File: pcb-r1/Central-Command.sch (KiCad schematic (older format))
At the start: 16 parts, among them P1 CONN_01X06, P2 CONN_01X02, P3 CONN_01X03, SW1 SW_PUSH, U1 STM32F030C8, Y1 Crystal

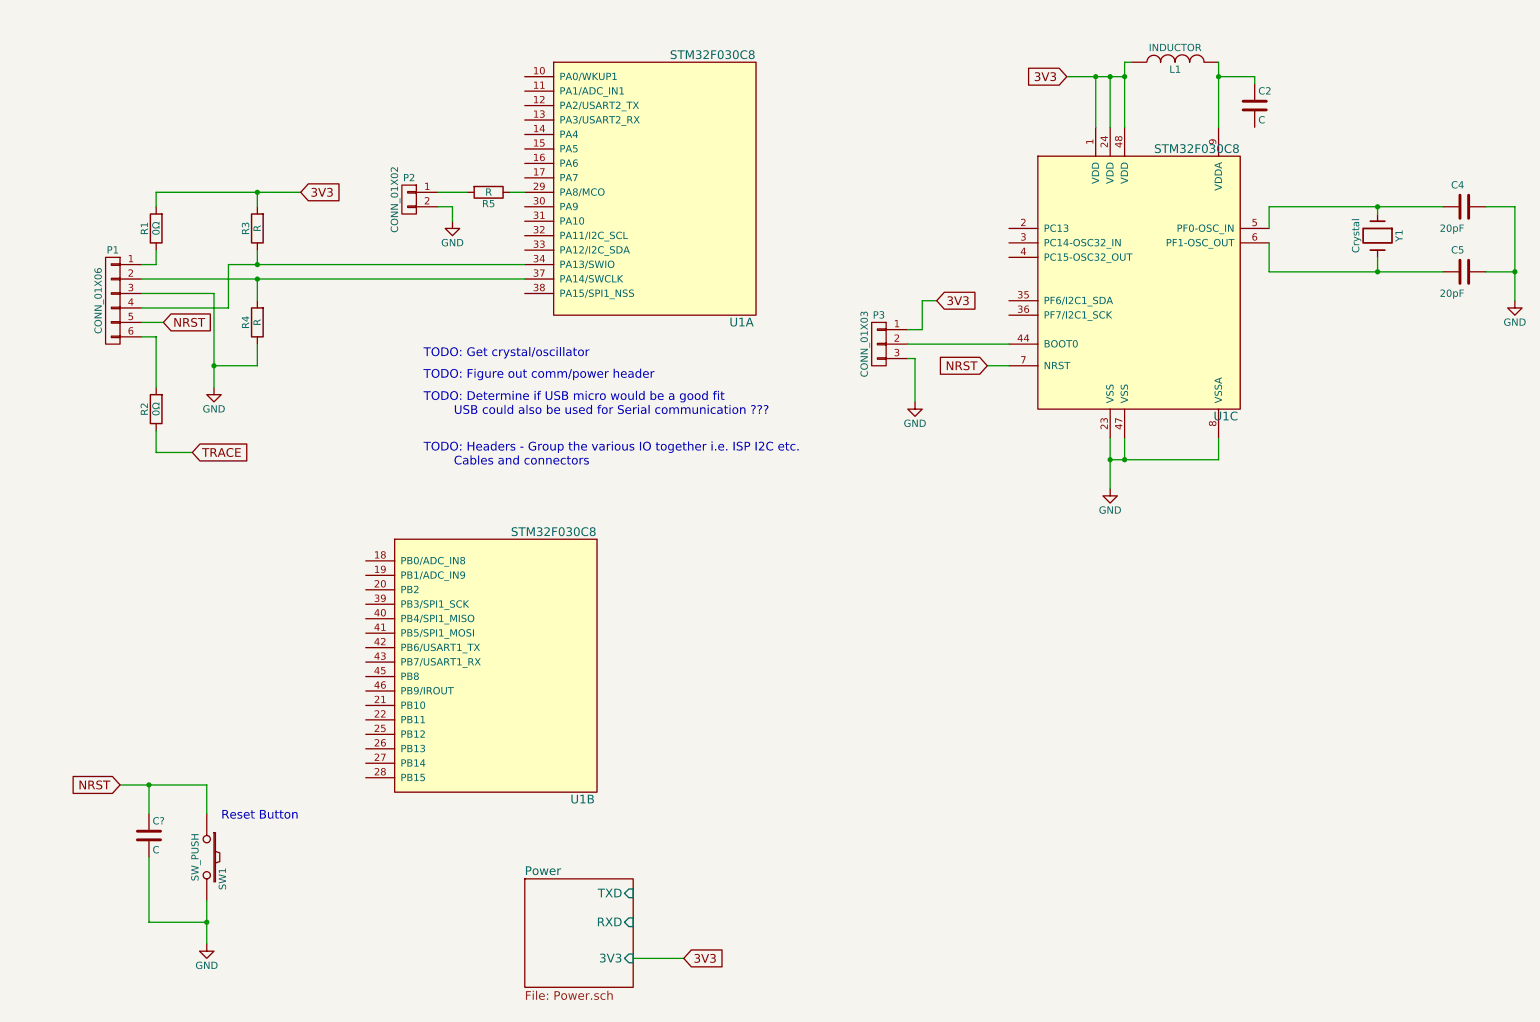
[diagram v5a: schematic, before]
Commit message: Updated the schematic with the latest from CC17
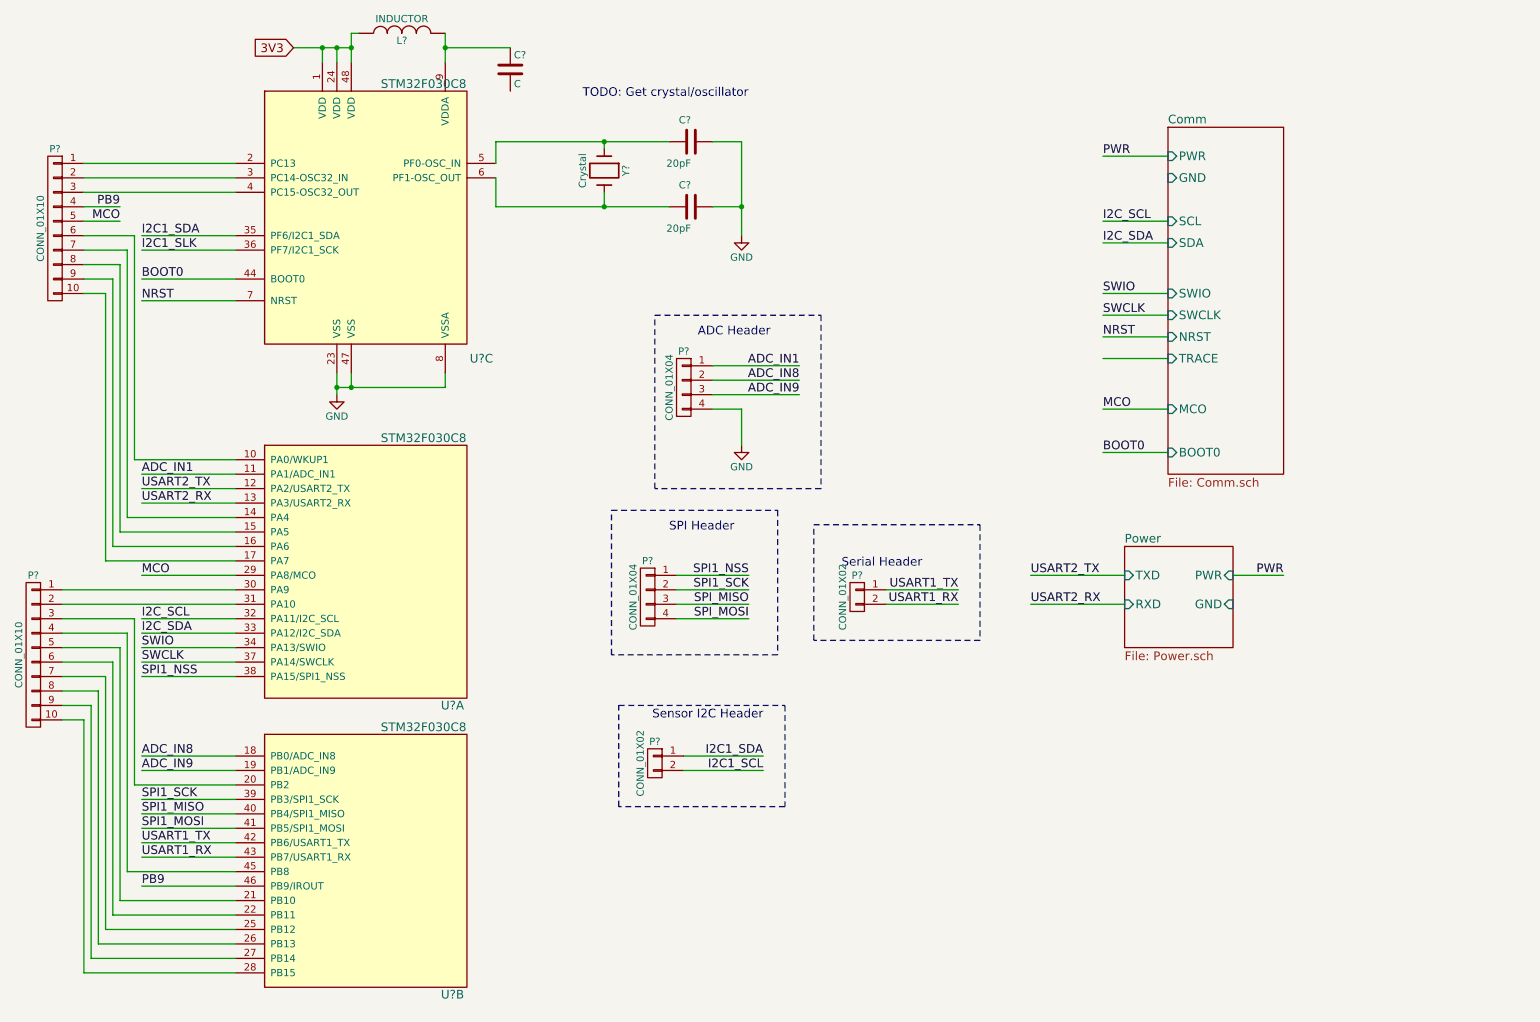
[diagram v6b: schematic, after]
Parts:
- removed C?: C, symbol C
- removed P1: CONN_01X06, Pin_Headers:Pin_Header_Straight_1x06, symbol CONN_01X06
- removed P2: CONN_01X02, Pin_Headers:Pin_Header_Straight_1x02, symbol CONN_01X02
- removed P3: CONN_01X03, symbol CONN_01X03
- removed R1, R2: 0Ω, Resistors_SMD:R_0805, symbol R
- removed R3, R4, R5: R, Resistors_SMD:R_0805, symbol R
- removed SW1: SW_PUSH, symbol SW_PUSH
- added P? (x2): CONN_01X10, symbol CONN_01X10
- added P? (x2): CONN_01X04, symbol CONN_01X04
- added P? (x2): CONN_01X02, symbol CONN_01X02
- renumbered C2 to C?, C5 to C?, C4 to C?, L1 to L?, U1 to U?, Y1 to Y?
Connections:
- net GND: now also P?.4 (P4)
- net at U?.10 (PA0/WKUP1): now also P?.6 (P6)
- net ADC_IN1: now reaches U?.11 (PA1/ADC_IN1)
- net ADC_IN1: now also P?.1 (P1)
- net USART2_TX: now reaches U?.12 (PA2/USART2_TX)
- net USART2_RX: now reaches U?.13 (PA3/USART2_RX)
- net at U?.14 (PA4): now also P?.7 (P7)
- net at U?.15 (PA5): now also P?.8 (P8)
- net at U?.16 (PA6): now also P?.9 (P9)
- net at U?.17 (PA7): now also P?.10 (P10)
- net MCO: now reaches U?.29 (PA8/MCO)
- net MCO: now also P?.5 (P5)
- net at U?.30 (PA9): now also P?.1 (P1)
- net at U?.31 (PA10): now also P?.2 (P2)
- net I2C_SCL: now reaches U?.32 (PA11/I2C_SCL)
- net I2C_SDA: now reaches U?.33 (PA12/I2C_SDA)
- net SWIO: now reaches U?.34 (PA13/SWIO)
- net SWCLK: now reaches U?.37 (PA14/SWCLK)
- net SPI1_NSS: now reaches U?.38 (PA15/SPI1_NSS)
- net SPI1_NSS: now also P?.1 (P1)
- net ADC_IN8: now reaches U?.18 (PB0/ADC_IN8)
- net ADC_IN8: now also P?.2 (P2)
- net ADC_IN9: now reaches U?.19 (PB1/ADC_IN9)
- net ADC_IN9: now also P?.3 (P3)
- net at U?.20 (PB2): now also P?.3 (P3)
- net at U?.21 (PB10): now also P?.5 (P5)
- net at U?.22 (PB11): now also P?.6 (P6)
- net at U?.25 (PB12): now also P?.7 (P7)
- net at U?.26 (PB13): now also P?.8 (P8)
- net at U?.27 (PB14): now also P?.9 (P9)
- net at U?.28 (PB15): now also P?.10 (P10)
- net SPI1_SCK: now reaches U?.39 (PB3/SPI1_SCK)
- net SPI1_SCK: now also P?.2 (P2)
- net SPI1_MISO: now reaches U?.40 (PB4/SPI1_MISO)
- net SPI1_MOSI: now reaches U?.41 (PB5/SPI1_MOSI)
- net USART1_TX: now reaches U?.42 (PB6/USART1_TX)
- net USART1_TX: now also P?.1 (P1)
- net USART1_RX: now reaches U?.43 (PB7/USART1_RX)
- net USART1_RX: now also P?.2 (P2)
- net at U?.45 (PB8): now also P?.4 (P4)
- net PB9: now reaches U?.46 (PB9/IROUT)
- net PB9: now also P?.4 (P4)
- net at U?.2 (PC13): now also P?.1 (P1)
- net at U?.3 (PC14-OSC32_IN): now also P?.2 (P2)
- net I2C1_SDA: now reaches U?.35 (PF6/I2C1_SDA)
- net I2C1_SDA: now also P?.1 (P1)
- net I2C1_SLK: now reaches U?.36 (PF7/I2C1_SCK)
- net at U?.4 (PC15-OSC32_OUT): now also P?.3 (P3)
- net BOOT0: now reaches U?.44 (BOOT0)
- new net I2C1_SCL: P?.2 (P2)
- new net SPI_MISO: P?.3 (P3)
- new net SPI_MOSI: P?.4 (P4)
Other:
- note added: "ADC Header"
- note added: "SPI Header"
- note added: "Sensor I2C Header"
- note added: "Serial Header"
- note removed: "Reset Button"
- note removed: "TODO: Determine if USB micro would be a good fit\n USB could also be used for Serial communication ???"
- note removed: "TODO: Figure out comm/power header"
- note removed: "TODO: Headers - Group the various IO together i.e. ISP I2C etc.\n Cables and connectors"
- moved on the sheet: C?, L?, U?A, U?B, U?C, Y?

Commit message: Edited the Central-Command.sch and forced the order of the hierarchical sheets to match the reference schematic annotations. Also annotated
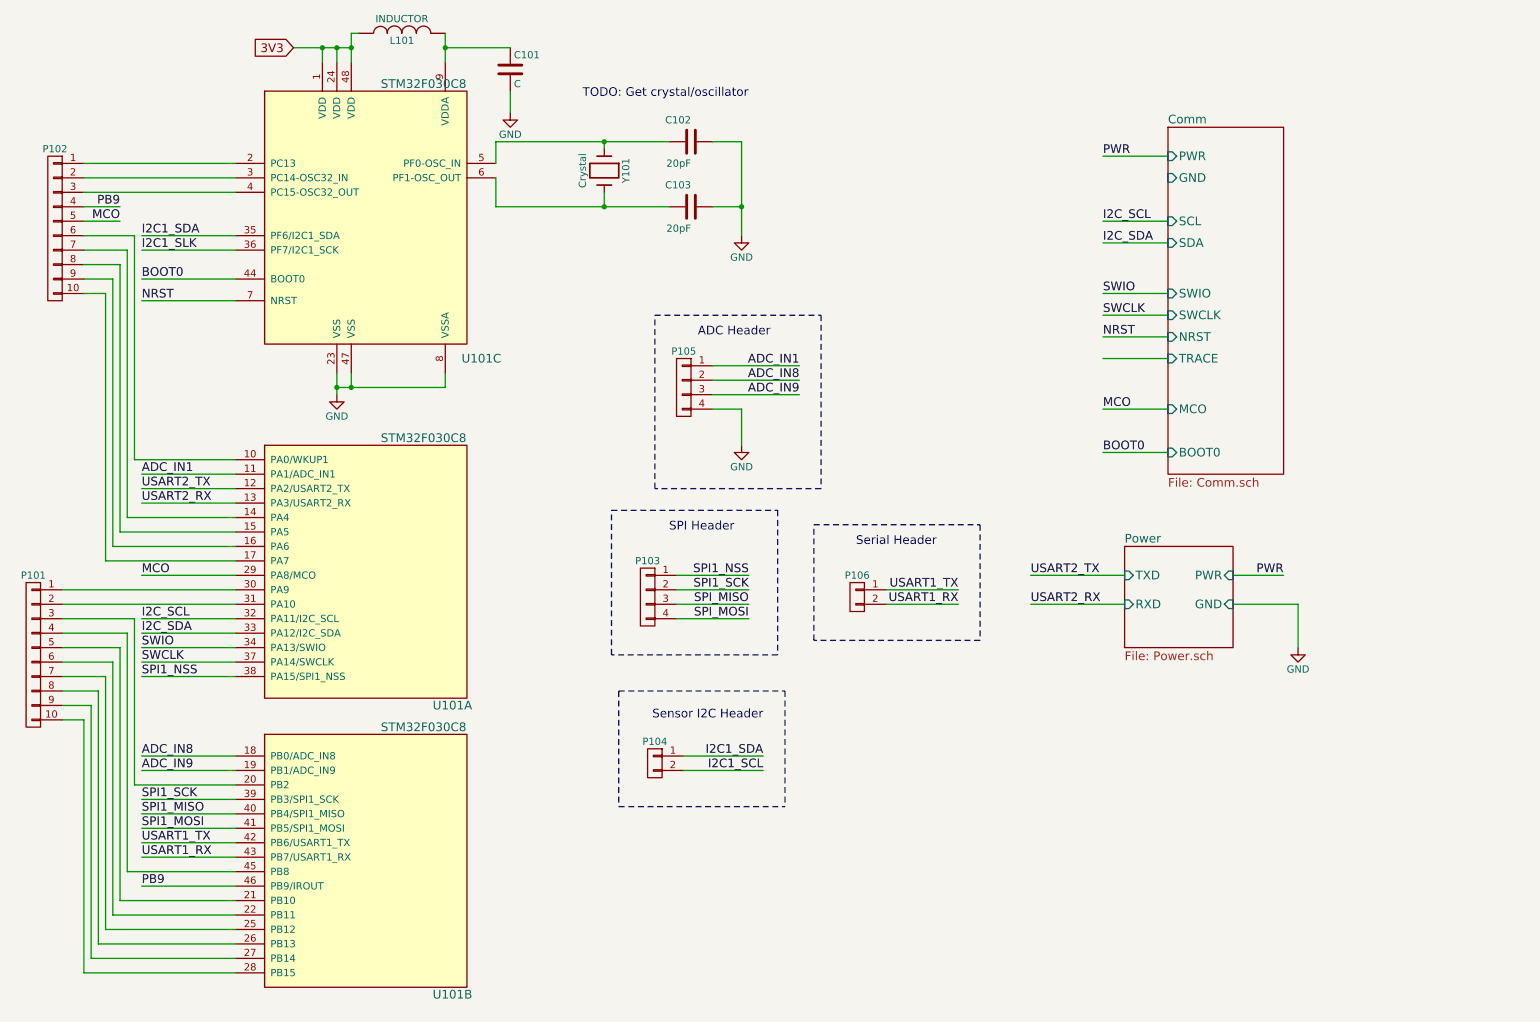
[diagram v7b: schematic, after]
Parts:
- gave numbers to parts that had none: 12
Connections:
- net GND: now also C101.2
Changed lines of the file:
@@
 $EndDescr
 $Comp
-L STM32F030C8 U?
+L STM32F030C8 U101
 U 1 1 5636B029
 P 3050 4500
-F 0 "U?" H 3600 3550 60  0000 C CNN
+F 0 "U101" H 3600 3550 60  0000 C CNN
 F 1 "STM32F030C8" H 3400 5400 60  0000 C CNN
 F 2 "Housings_QFP:LQFP-48_7x7mm_Pitch0.5mm" H 3050 4500 60  0001 C CNN
@@
 $EndComp
 $Comp
-L STM32F030C8 U?
+L STM32F030C8 U101
 U 2 1 5636B0CD
 P 3050 6500
-F 0 "U?" H 3600 5550 60  0000 C CNN
+F 0 "U101" H 3600 5550 60  0000 C CNN
 F 1 "STM32F030C8" H 3400 7400 60  0000 C CNN
 F 2 "Housings_QFP:LQFP-48_7x7mm_Pitch0.5mm" H 3050 6500 60  0001 C CNN
@@
 $EndComp
 $Comp
-L STM32F030C8 U?
+L STM32F030C8 U101
 U 3 1 5636B111
 P 3050 2050
-F 0 "U?" H 3800 1050 60  0000 C CNN
+F 0 "U101" H 3800 1050 60  0000 C CNN
 F 1 "STM32F030C8" H 3400 2950 60  0000 C CNN
 F 2 "Housings_QFP:LQFP-48_7x7mm_Pitch0.5mm" H 3050 2050 60  0001 C CNN
@@
 $EndComp
 $Comp
-L INDUCTOR L?
+L INDUCTOR L101
 U 1 1 5636B065
 P 3250 800
-F 0 "L?" V 3200 800 50  0000 C CNN
+F 0 "L101" V 3200 800 50  0000 C CNN
 F 1 "INDUCTOR" V 3350 800 50  0000 C CNN
 F 2 "Inductors_NEOSID:Neosid_Inductor_SM1206" H 3250 800 60  0001 C CNN
@@
 $EndComp
 $Comp
-L C C?
+L C C101
 U 1 1 5636B131
 P 4000 1050
-F 0 "C?" H 4025 1150 50  0000 L CNN
+F 0 "C101" H 4025 1150 50  0000 L CNN
 F 1 "C" H 4025 950 50  0000 L CNN
 F 2 "Capacitors_SMD:C_0805" H 4038 900 30  0001 C CNN
@@
 $EndComp
 $Comp
-L GND #PWR?
+L GND #PWR101
 U 1 1 5636B68F
 P 2800 3300
-F 0 "#PWR?" H 2800 3050 50  0001 C CNN
+F 0 "#PWR101" H 2800 3050 50  0001 C CNN
 F 1 "GND" H 2800 3150 50  0000 C CNN
 F 2 "" H 2800 3300 60  0000 C CNN
@@
 TODO: Get crystal/oscillator
 $Comp
-L Crystal Y?
+L Crystal Y101
 U 1 1 5654A44B
 P 4650 1750
-F 0 "Y?" H 4650 1900 50  0000 C CNN
+F 0 "Y101" H 4650 1900 50  0000 C CNN
 F 1 "Crystal" H 4650 1600 50  0000 C CNN
 F 2 "" H 4650 1750 60  0000 C CNN
@@
 $EndComp
 $Comp
-L C C?
+L C C103
 U 1 1 5654A4FC
 P 5250 2000
-F 0 "C?" V 5400 2000 50  0000 L CNN
+F 0 "C103" V 5400 2000 50  0000 L CNN
 F 1 "20pF" V 5100 2000 50  0000 L CNN
 F 2 "" H 5288 1850 30  0000 C CNN
@@
 $EndComp
 $Comp
-L C C?
+L C C102
 U 1 1 5654A5C1
 P 5250 1550
-F 0 "C?" V 5400 1550 50  0000 L CNN
+F 0 "C102" V 5400 1550 50  0000 L CNN
 F 1 "20pF" V 5100 1550 50  0000 L CNN
 F 2 "" H 5288 1400 30  0000 C CNN
@@
 $EndComp
 $Comp
-L GND #PWR?
+L GND #PWR102
 U 1 1 5654AC7D
 P 5600 2200
-F 0 "#PWR?" H 5600 1950 50  0001 C CNN
+F 0 "#PWR102" H 5600 1950 50  0001 C CNN
 F 1 "GND" H 5600 2050 50  0000 C CNN
 F 2 "" H 5600 2200 60  0000 C CNN
@@
 	1    0    0    -1
 $EndComp
-$Sheet
-S 8250 4350 750  700
-U 5657EAAA
-F0 "Power" 60
-F1 "Power.sch" 60
-F2 "TXD" I L 8250 4550 60
-F3 "RXD" I L 8250 4750 60
-F4 "PWR" I R 9000 4550 60
-F5 "GND" I R 9000 4750 60
-$EndSheet
-Text Label 9350 4550 2    60   ~ 0
-PWR
 $Sheet
 S 8550 1450 800  2400
@@
 Text Label 8100 3700 0    60   ~ 0
 BOOT0
-$Comp
-L CONN_01X10 P?
+$Sheet
+S 8250 4350 750  700
+U 5657EAAA
+F0 "Power" 60
+F1 "Power.sch" 60
+F2 "TXD" I L 8250 4550 60
+F3 "RXD" I L 8250 4750 60
+F4 "PWR" I R 9000 4550 60
+F5 "GND" I R 9000 4750 60
+$EndSheet
+Text Label 9350 4550 2    60   ~ 0
+PWR
+$Comp
+L CONN_01X10 P101
 U 1 1 56677880
 P 700 5100
-F 0 "P?" H 700 5650 50  0000 C CNN
-F 1 "CONN_01X10" V 800 5100 50  0000 C CNN
+F 0 "P101" H 700 5650 50  0000 C CNN
+F 1 "CONN_01X10" V 800 5100 50  0001 C CNN
 F 2 "" H 700 5100 60  0000 C CNN
 F 3 "" H 700 5100 60  0000 C CNN
@@
 NRST
 $Comp
-L CONN_01X10 P?
+L CONN_01X10 P102
 U 1 1 5667B794
 P 850 2150
-F 0 "P?" H 850 2700 50  0000 C CNN
-F 1 "CONN_01X10" V 950 2150 50  0000 C CNN
+F 0 "P102" H 850 2700 50  0000 C CNN
+F 1 "CONN_01X10" V 950 2150 50  0001 C CNN
 F 2 "" H 850 2150 60  0000 C CNN
 F 3 "" H 850 2150 60  0000 C CNN
@@
 MCO
 $Comp
-L CONN_01X04 P?
+L CONN_01X04 P105
 U 1 1 5667E55B
 P 5200 3250
-F 0 "P?" H 5200 3500 50  0000 C CNN
-F 1 "CONN_01X04" V 5300 3250 50  0000 C CNN
+F 0 "P105" H 5200 3500 50  0000 C CNN
+F 1 "CONN_01X04" V 5300 3250 50  0001 C CNN
 F 2 "" H 5200 3250 60  0000 C CNN
 F 3 "" H 5200 3250 60  0000 C CNN
@@
 $EndComp
 $Comp
-L GND #PWR?
+L GND #PWR103
 U 1 1 5667E90C
 P 5600 3650
-F 0 "#PWR?" H 5600 3400 50  0001 C CNN
+F 0 "#PWR103" H 5600 3400 50  0001 C CNN
 F 1 "GND" H 5600 3500 50  0000 C CNN
 F 2 "" H 5600 3650 60  0000 C CNN
@@
 ADC Header
 $Comp
-L CONN_01X04 P?
+L CONN_01X04 P103
 U 1 1 5667EF67
 P 4950 4700
-F 0 "P?" H 4950 4950 50  0000 C CNN
-F 1 "CONN_01X04" V 5050 4700 50  0000 C CNN
+F 0 "P103" H 4950 4950 50  0000 C CNN
+F 1 "CONN_01X04" V 5050 4700 50  0001 C CNN
 F 2 "" H 4950 4700 60  0000 C CNN
 F 3 "" H 4950 4700 60  0000 C CNN
@@
 SPI Header
 $Comp
-L CONN_01X02 P?
+L CONN_01X02 P106
 U 1 1 5667FC37
 P 6400 4700
-F 0 "P?" H 6400 4850 50  0000 C CNN
-F 1 "CONN_01X02" V 6500 4700 50  0000 C CNN
+F 0 "P106" H 6400 4850 50  0000 C CNN
+F 1 "CONN_01X02" V 6500 4700 50  0001 C CNN
 F 2 "" H 6400 4700 60  0000 C CNN
 F 3 "" H 6400 4700 60  0000 C CNN
@@
 Text Label 7100 4750 2    60   ~ 0
 USART1_RX
-Text Notes 6850 4500 2    60   ~ 0
+Text Notes 6950 4350 2    60   ~ 0
 Serial Header
 $Comp
-L CONN_01X02 P?
+L CONN_01X02 P104
 U 1 1 5668077B
 P 5000 5850
-F 0 "P?" H 5000 6000 50  0000 C CNN
-F 1 "CONN_01X02" V 5100 5850 50  0000 C CNN
+F 0 "P104" H 5000 6000 50  0000 C CNN
+F 1 "CONN_01X02" V 5100 5850 50  0001 C CNN
 F 2 "" H 5000 5850 60  0000 C CNN
 F 3 "" H 5000 5850 60  0000 C CNN
@@
 	3550 900  4000 900
 Wire Wire Line
-	2800 3150 2800 3250
-Wire Wire Line
-	2800 3250 2800 3300
+	2800 3150 2800 3300
 Wire Wire Line
 	2900 3150 2900 3250
 Wire Wire Line
-	2800 3250 2900 3250
-Wire Wire Line
-	2900 3250 3550 3250
+	2800 3250 3550 3250
 Connection ~ 2800 3250
 Wire Wire Line
@@
 Connection ~ 2900 3250
 Wire Wire Line
-	2500 900  2700 900
-Wire Wire Line
-	2700 900  2800 900
-Wire Wire Line
-	2800 900  2900 900
-Wire Wire Line
-	2900 800  2900 900
-Wire Wire Line
-	2900 900  2900 1000
-Wire Wire Line
-	3550 800  3550 900
-Wire Wire Line
-	3550 900  3550 1000
+	2500 900  2900 900
+Wire Wire Line
+	2900 800  2900 1000
+Wire Wire Line
+	3550 800  3550 1000
 Wire Wire Line
 	2700 1000 2700 900
@@
 	3900 1700 3900 1550
 Wire Wire Line
-	3900 1550 4650 1550
-Wire Wire Line
-	4650 1550 5100 1550
+	3900 1550 5100 1550
 Wire Wire Line
 	3900 1800 3900 2000
 Wire Wire Line
-	3900 2000 4650 2000
-Wire Wire Line
-	4650 2000 5100 2000
+	3900 2000 5100 2000
 Wire Wire Line
 	5400 1550 5600 1550
 Wire Wire Line
-	5600 1550 5600 2000
-Wire Wire Line
-	5600 2000 5600 2200
+	5600 1550 5600 2200
 Wire Wire Line
 	5600 2000 5400 2000
@@
 I2C1_SCL
 Wire Notes Line
-	4750 5450 5900 5450
-Wire Notes Line
-	5900 5450 5900 6150
-Wire Notes Line
-	5900 6150 4750 6150
-Wire Notes Line
-	4750 6150 4750 5450
+	4750 5350 5900 5350
+Wire Notes Line
+	5900 5350 5900 6150
+Wire Notes Line
+	4750 6150 5900 6150
+Wire Notes Line
+	4750 5350 4750 6150
 Text Notes 5750 5550 2    60   ~ 0
 Sensor I2C Header
@@
 Text Label 7600 4750 0    60   ~ 0
 USART2_RX
+$Comp
+L GND #PWR?
+U 1 1 56673817
+P 4000 1350
+F 0 "#PWR?" H 4000 1100 50  0001 C CNN
+F 1 "GND" H 4000 1200 50  0000 C CNN
+F 2 "" H 4000 1350 60  0000 C CNN
+F 3 "" H 4000 1350 60  0000 C CNN
+	1    4000 1350
+	1    0    0    -1
+$EndComp
+Wire Wire Line
+	4000 1200 4000 1350
+$Comp
+L GND #PWR?
+U 1 1 56673B6E
+P 9450 5050
+F 0 "#PWR?" H 9450 4800 50  0001 C CNN
+F 1 "GND" H 9450 4900 50  0000 C CNN
+F 2 "" H 9450 5050 60  0000 C CNN
+F 3 "" H 9450 5050 60  0000 C CNN
+	1    9450 5050
+	1    0    0    -1
+$EndComp
+Wire Wire Line
+	9000 4750 9450 4750
+Wire Wire Line
+	9450 4750 9450 5050
 $EndSCHEMATC
